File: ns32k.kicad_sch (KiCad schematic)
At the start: 46 parts, among them SW2 SW_DIP_x04 300w/50p mil, U1 NS32201, U10 74AHC373, U11 74AHC373, U12 74AHC138, U13 AS6C6416-55, U15 MX29LV040C DNP, U16 MX29LV040C DNP, U19 74AHC32, U20 74AHC1GU04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

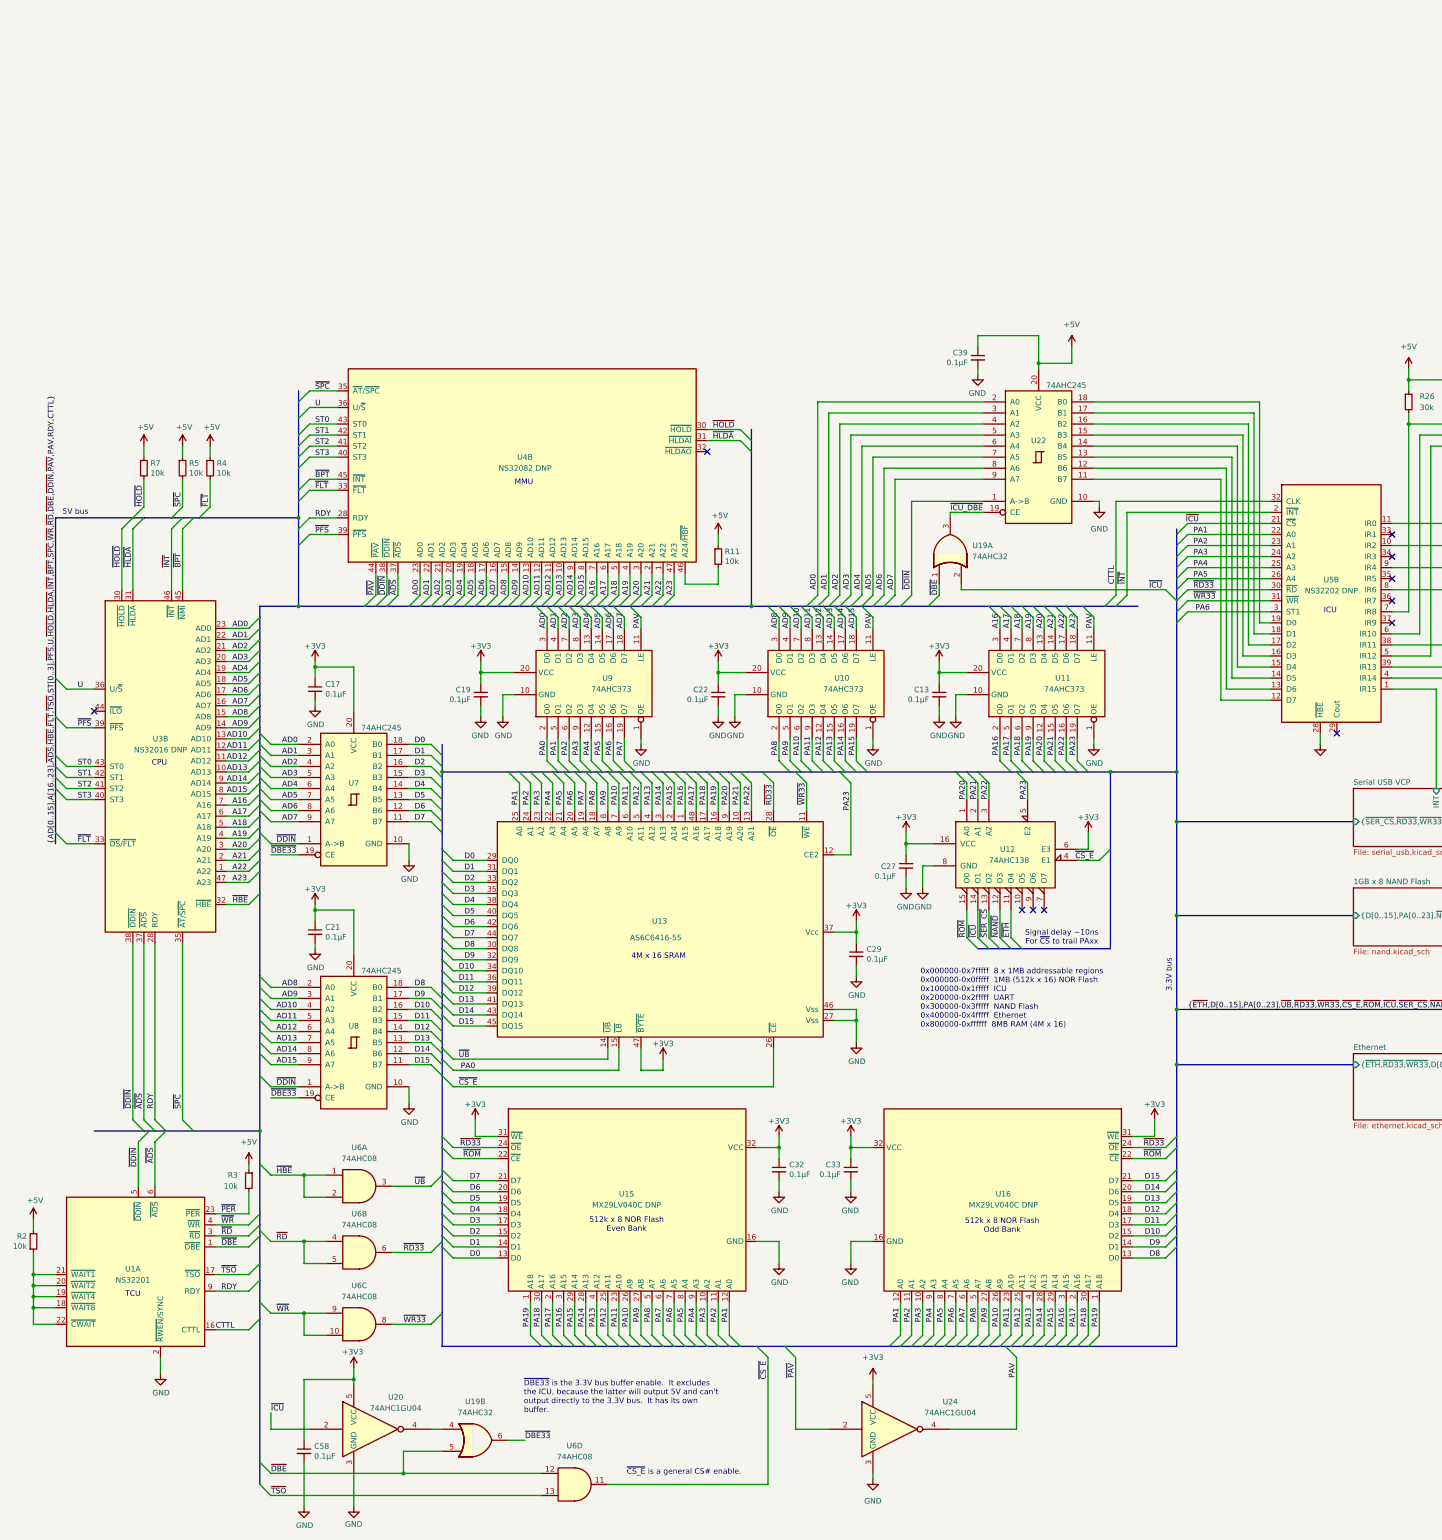
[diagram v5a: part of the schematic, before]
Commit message: various changes, add LCSC part #s
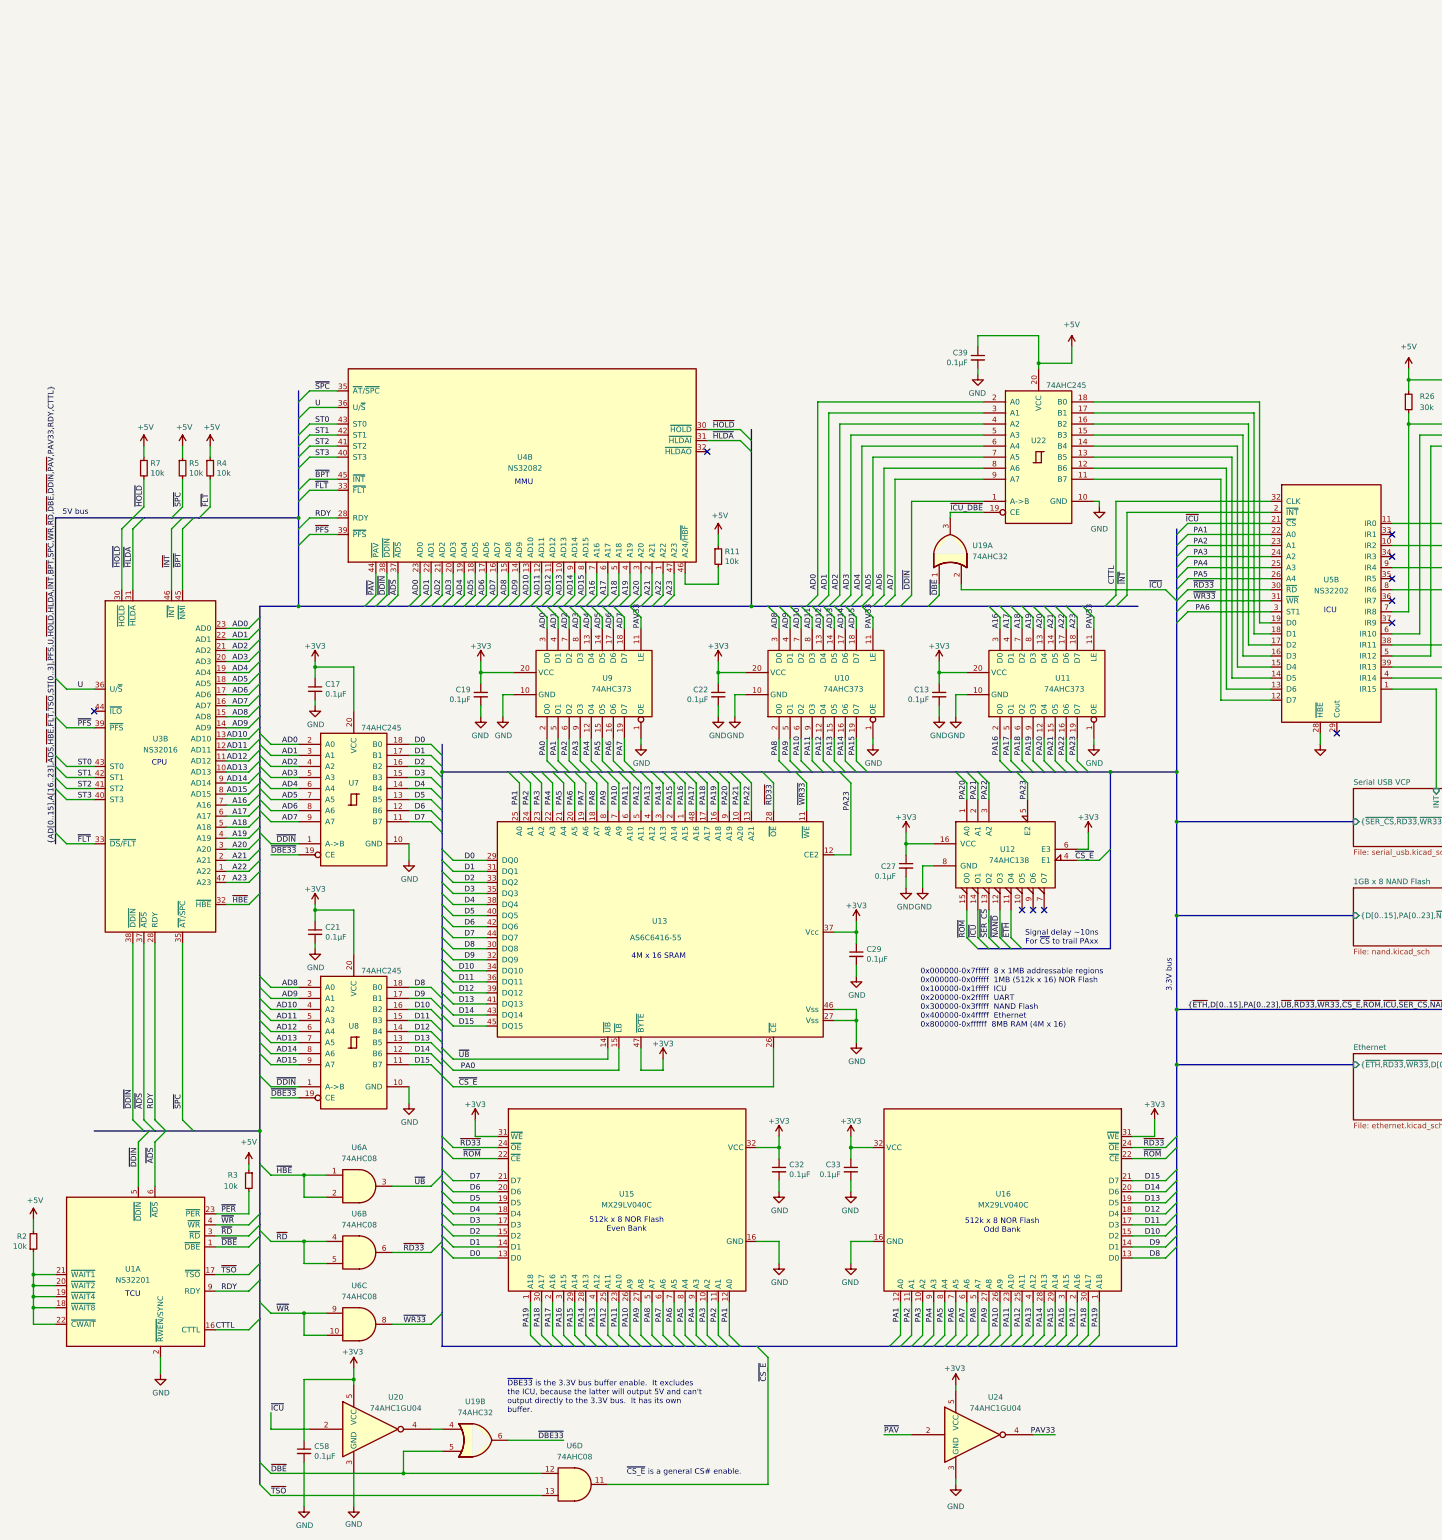
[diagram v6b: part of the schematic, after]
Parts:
- C13, C17, C19, C21, C22, C27, C29, C32, C33, C39, C58: LCSC C466613 -> C3012376
- U15, U16: value MX29LV040C DNP -> MX29LV040C
- U20, U24: LCSC C352954 -> C22384791
- U3: value NS32016 DNP -> NS32016
- U4: value NS32082 DNP -> NS32082
- U5: value NS32202 DNP -> NS32202
- U6: LCSC C2863502 -> C842279
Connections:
- net PAV renamed PAV33
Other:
- moved on the sheet: U24

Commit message: fix a few bugs
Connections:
- net ~{ADS}: no longer U1.6 (~{ADS})
- net ~{PAV}: now also U1.6 (~{ADS})
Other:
- title: NS32016 Toy PCB -> Toy32k
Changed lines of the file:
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@@
 	(paper "A3")
 	(title_block
-		(title "NS32016 Toy PCB")
-		(date "2024-08-10")
-		(rev "Rev 4")
+		(title "Toy32k")
+		(date "2024-08-16")
+		(rev "Rev 5")
 		(comment 1 "bson@rockgarden.net")
 		(comment 2 "Jan Brittenson")
@@
 		)
 	)
-	(label "~{ADS}"
+	(label "~{PAV}"
 		(at 58.42 200.66 270)
 		(fields_autoplaced yes)
